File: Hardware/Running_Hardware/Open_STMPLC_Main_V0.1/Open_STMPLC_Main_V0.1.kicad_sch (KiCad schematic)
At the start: 0 parts

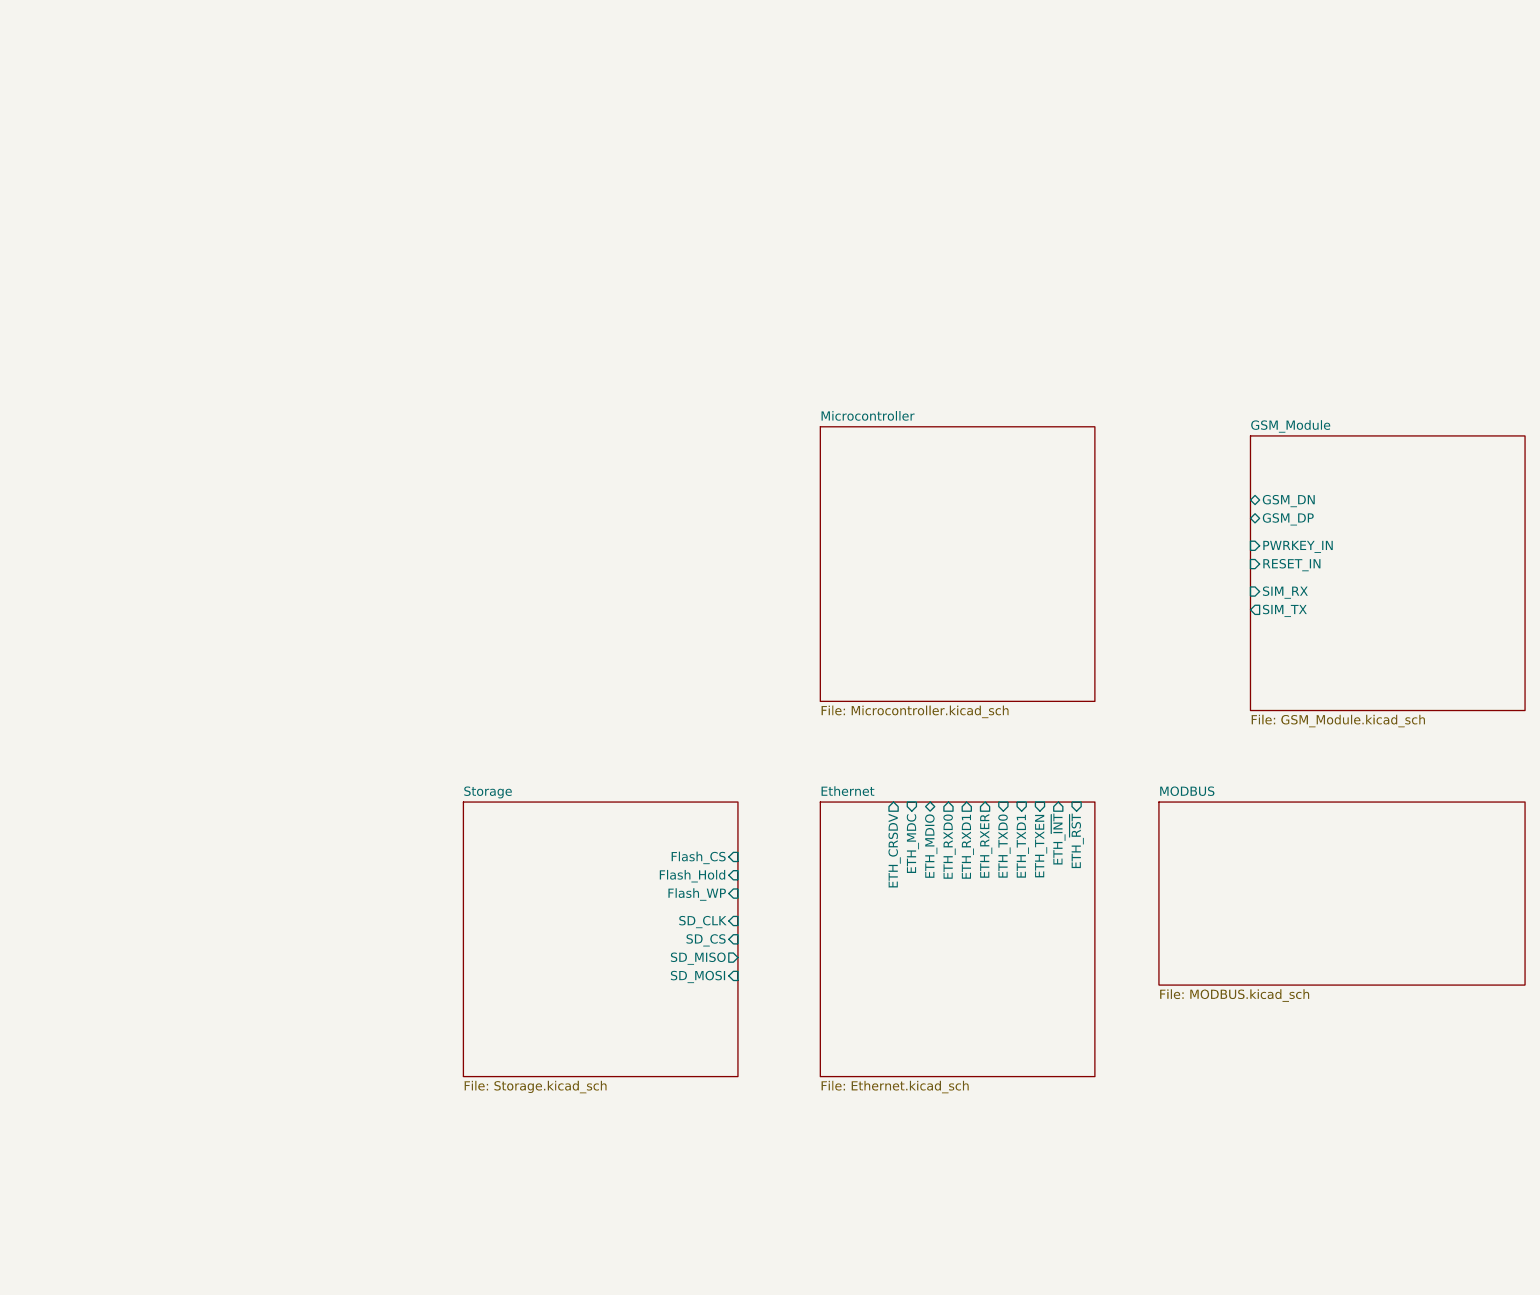
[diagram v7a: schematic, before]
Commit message: Main PCB schematic changes V0.1
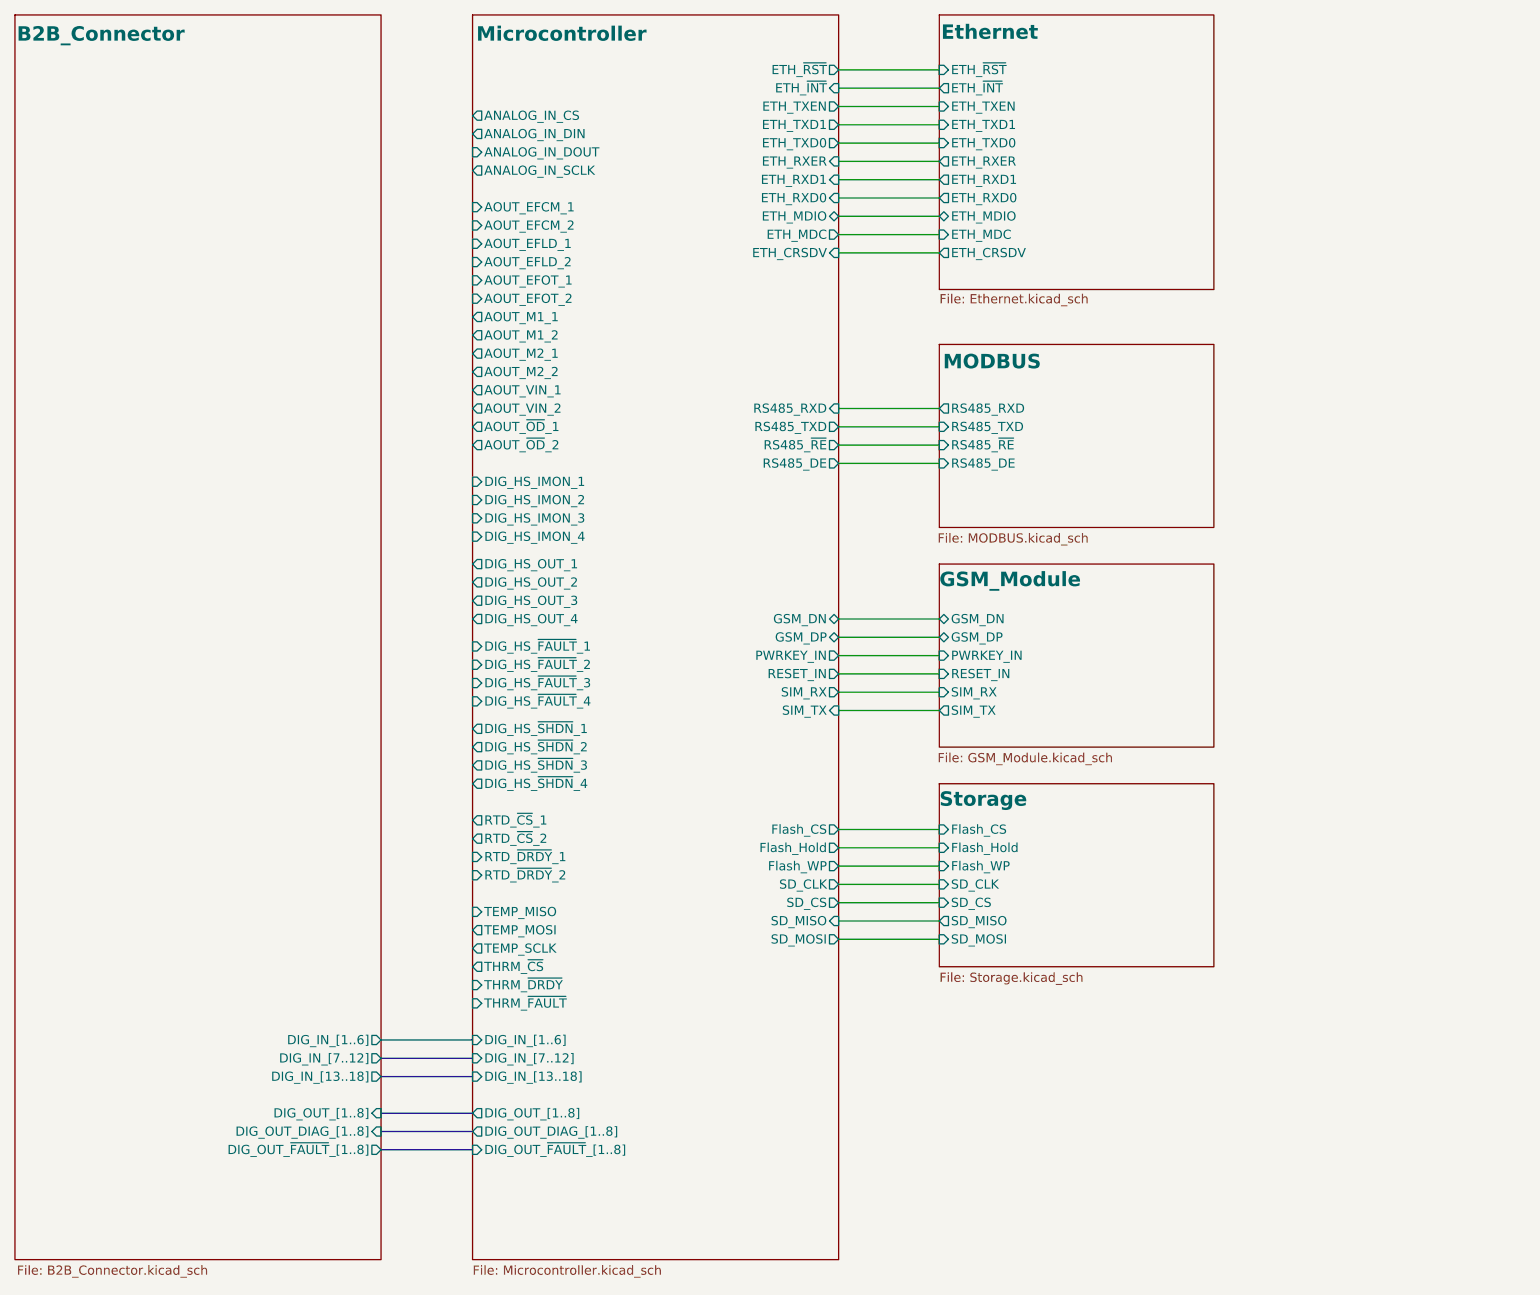
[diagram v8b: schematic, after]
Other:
- added sheet B2B_Connector (B2B_Connector.kicad_sch)
- sheet MODBUS ports: added RS485_DE, RS485_RXD, RS485_TXD, RS485_~{RE}; removed none
- sheet Microcontroller ports: added ANALOG_IN_CS, ANALOG_IN_DIN, ANALOG_IN_DOUT, ANALOG_IN_SCLK, AOUT_EFCM_1, AOUT_EFCM_2, AOUT_EFLD_1, AOUT_EFLD_2, AOUT_EFOT_1, AOUT_EFOT_2, AOUT_M1_1, AOUT_M1_2, AOUT_M2_1, AOUT_M2_2, AOUT_VIN_1, AOUT_VIN_2, AOUT_~{OD}_1, AOUT_~{OD}_2, DIG_HS_IMON_1, DIG_HS_IMON_2, DIG_HS_IMON_3, DIG_HS_IMON_4, DIG_HS_OUT_1, DIG_HS_OUT_2, DIG_HS_OUT_3, DIG_HS_OUT_4, DIG_HS_~{FAULT}_1, DIG_HS_~{FAULT}_2, DIG_HS_~{FAULT}_3, DIG_HS_~{FAULT}_4, DIG_HS_~{SHDN}_1, DIG_HS_~{SHDN}_2, DIG_HS_~{SHDN}_3, DIG_HS_~{SHDN}_4, DIG_IN_[1..6], DIG_IN_[13..18], DIG_IN_[7..12], DIG_OUT_DIAG_[1..8], DIG_OUT_[1..8], DIG_OUT_~{FAULT}_[1..8], ETH_CRSDV, ETH_MDC, ETH_MDIO, ETH_RXD0, ETH_RXD1, ETH_RXER, ETH_TXD0, ETH_TXD1, ETH_TXEN, ETH_~{INT}, ETH_~{RST}, Flash_CS, Flash_Hold, Flash_WP, GSM_DN, GSM_DP, PWRKEY_IN, RESET_IN, RS485_DE, RS485_RXD, RS485_TXD, RS485_~{RE}, RTD_~{CS}_1, RTD_~{CS}_2, RTD_~{DRDY}_1, RTD_~{DRDY}_2, SD_CLK, SD_CS, SD_MISO, SD_MOSI, SIM_RX, SIM_TX, TEMP_MISO, TEMP_MOSI, TEMP_SCLK, THRM_~{CS}, THRM_~{DRDY}, THRM_~{FAULT}; removed none
- title: (none) -> Open_STMPLC_Main
